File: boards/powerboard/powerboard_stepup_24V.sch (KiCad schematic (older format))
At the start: 22 parts

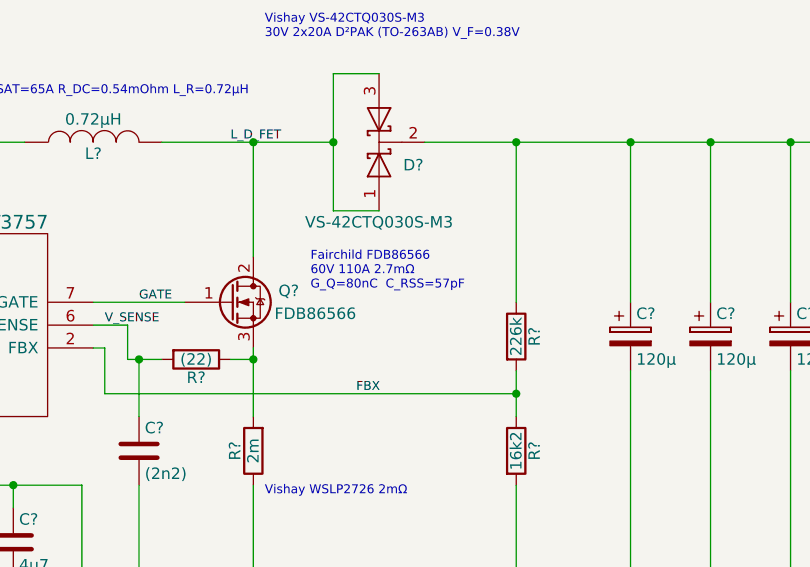
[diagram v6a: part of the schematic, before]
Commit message: [powerboard] various fixes (charge circuit, boost converter, 5V buck regulator)
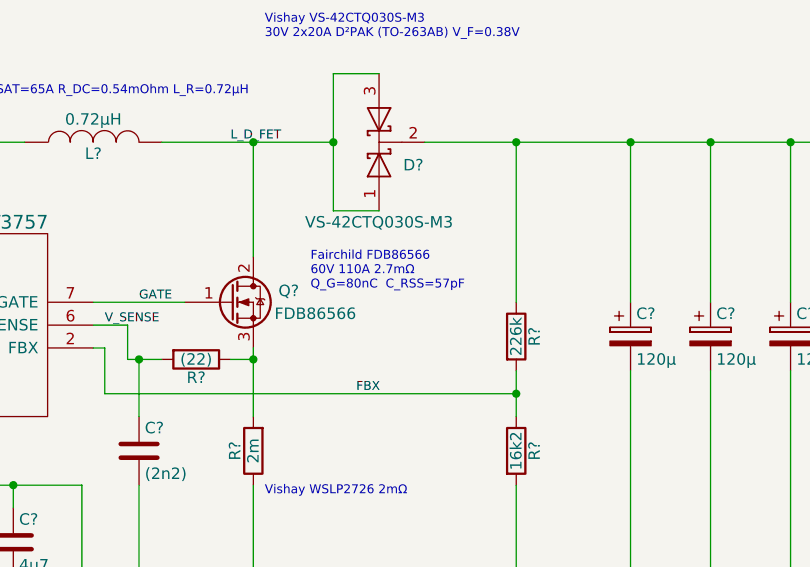
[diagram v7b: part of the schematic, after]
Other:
- note added: "Fairchild FDB86566\n60V 110A 2.7mΩ\nQ_G=80nC C_RSS=57pF"
- note removed: "Fairchild FDB86566\n60V 110A 2.7mΩ\nG_Q=80nC C_RSS=57pF"
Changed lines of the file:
@@
 $EndComp
 Text Notes 6150 1950 0    39   ~ 0
-Fairchild FDB86566\n60V 110A 2.7mΩ\nG_Q=80nC  C_RSS=57pF
+Fairchild FDB86566\n60V 110A 2.7mΩ\nQ_G=80nC  C_RSS=57pF
 Text Label 5250 2100 0    39   ~ 0
 V_SENSE
